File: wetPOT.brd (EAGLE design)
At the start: 38.1 x 12.7 mm, 2 parts

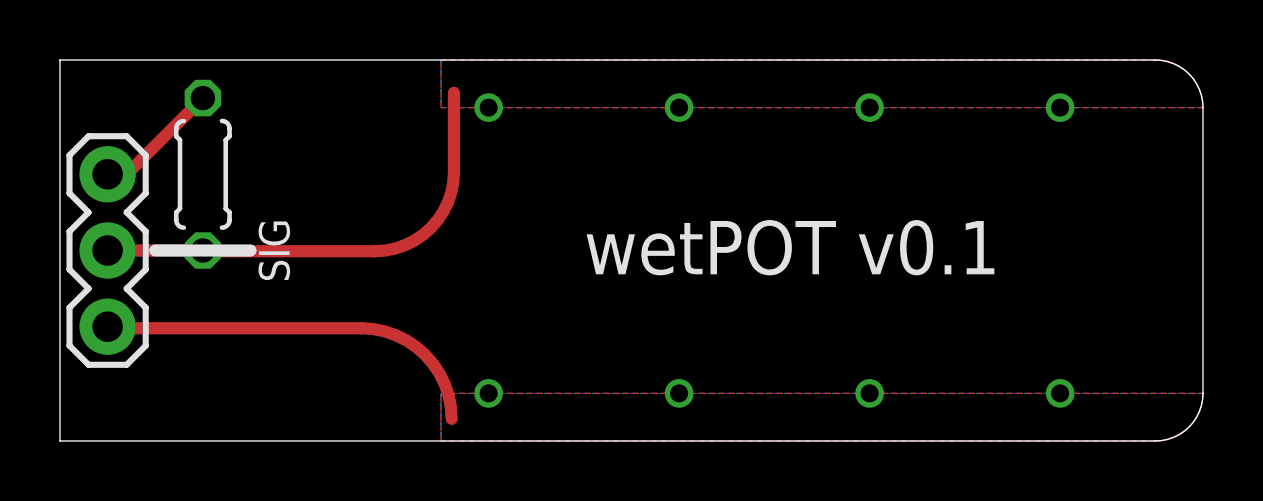
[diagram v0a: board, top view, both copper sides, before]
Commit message: Swap pin0 & pin1 to match servo wiring (Ground, VCC, Sig)
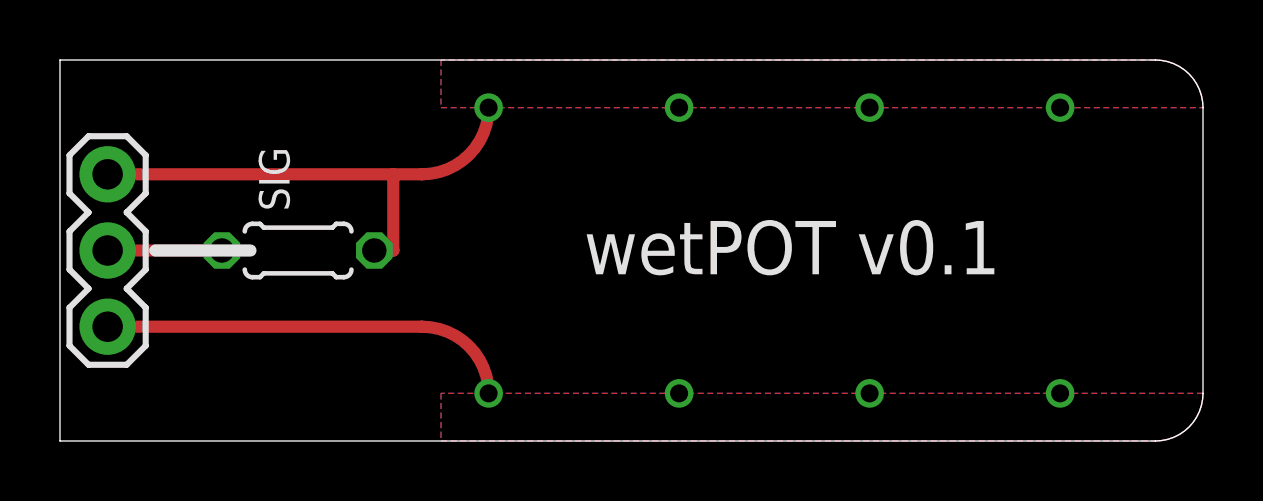
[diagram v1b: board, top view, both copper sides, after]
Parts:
- moved R1 4.07 mm to (7.94, 6.35), turned to 0 degrees
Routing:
- net PIN0: track 4.23 -> 16.8 mm, vias 0 -> 4
- net PIN1: track 15.2 -> 3.81 mm, vias 4 -> 0
- net PIN2: track 12.6 -> 13.6 mm
- added copper zone on layer 1, net PIN0
- added copper zone on layer 16, net PIN0
- removed copper zone on layer 1, net PIN1
- removed copper zone on layer 16, net PIN1
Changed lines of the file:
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@@
 <layer number="27" name="tValues" color="7" fill="1" visible="yes" active="yes"/>
 <layer number="28" name="bValues" color="7" fill="1" visible="yes" active="yes"/>
-<layer number="29" name="tStop" color="7" fill="3" visible="yes" active="yes"/>
-<layer number="30" name="bStop" color="7" fill="6" visible="yes" active="yes"/>
+<layer number="29" name="tStop" color="7" fill="3" visible="no" active="yes"/>
+<layer number="30" name="bStop" color="7" fill="6" visible="no" active="yes"/>
 <layer number="31" name="tCream" color="7" fill="4" visible="yes" active="yes"/>
 <layer number="32" name="bCream" color="7" fill="5" visible="yes" active="yes"/>
@@
 <wire x1="36.5125" y1="12.7" x2="0" y2="12.7" width="0" layer="20"/>
 <wire x1="0" y1="12.7" x2="0" y2="0" width="0" layer="20"/>
-<text x="7.14375" y="6.35" size="1.016" layer="121" rot="R90" align="center">SIG</text>
+<text x="7.14375" y="8.73125" size="1.016" layer="121" rot="R90" align="center">SIG</text>
 <wire x1="3.175" y1="6.35" x2="6.35" y2="6.35" width="0.4064" layer="121"/>
 <text x="17.4625" y="5.55625" size="1.778" layer="121">wetPOT v0.1</text>
+<polygon width="0.4064" layer="29">
+<vertex x="12.7" y="1.5875"/>
+<vertex x="38.1" y="1.5875" curve="-90"/>
+<vertex x="36.5125" y="0"/>
+<vertex x="12.7" y="0"/>
+</polygon>
+<polygon width="0.4064" layer="30">
+<vertex x="12.7" y="1.5875"/>
+<vertex x="12.7" y="0"/>
+<vertex x="36.5125" y="0" curve="90"/>
+<vertex x="38.1" y="1.5875"/>
+</polygon>
+<text x="34.13125" y="4.7625" size="1.4224" layer="122" rot="MR0">andrewparnell.com
+CC: BY-SA</text>
+<polygon width="0.4064" layer="30">
+<vertex x="12.7" y="12.7"/>
+<vertex x="12.7" y="11.1125"/>
+<vertex x="38.1" y="11.1125" curve="90"/>
+<vertex x="36.5125" y="12.7"/>
+</polygon>
 <polygon width="0.4064" layer="29">
 <vertex x="12.7" y="12.7"/>
@@
 <vertex x="36.5125" y="12.7"/>
 </polygon>
-<polygon width="0.4064" layer="29">
-<vertex x="12.7" y="1.5875"/>
-<vertex x="38.1" y="1.5875" curve="-90"/>
-<vertex x="36.5125" y="0"/>
-<vertex x="12.7" y="0"/>
-</polygon>
-<polygon width="0.4064" layer="30">
-<vertex x="12.7" y="11.1125"/>
-<vertex x="12.7" y="12.7"/>
-<vertex x="36.5125" y="12.7" curve="-90"/>
-<vertex x="38.1" y="11.1125"/>
-</polygon>
-<polygon width="0.4064" layer="30">
-<vertex x="12.7" y="1.5875"/>
-<vertex x="12.7" y="0"/>
-<vertex x="36.5125" y="0" curve="90"/>
-<vertex x="38.1" y="1.5875"/>
-</polygon>
-<text x="34.13125" y="4.7625" size="1.4224" layer="122" rot="MR0">andrewparnell.com
-CC: BY-SA</text>
 </plain>
 <attributes>
@@
 </autorouter>
 <elements>
-<element name="R1" library="resistor" package="0204/5" value="10k" x="4.7625" y="8.89" smashed="yes" rot="R90"/>
+<element name="R1" library="resistor" package="0204/5" value="10k" x="7.9375" y="6.35" smashed="yes"/>
 <element name="JP2" library="SparkFun-Connectors" package="1X03" value="" x="1.5875" y="3.81" smashed="yes" rot="R90">
 <attribute name="VALUE" x="4.7625" y="2.54" size="1.27" layer="27" rot="R90"/>
@@
 <contactref element="R1" pad="2"/>
 <contactref element="JP2" pad="3"/>
-<wire x1="1.5875" y1="8.89" x2="2.2225" y2="8.89" width="0.4064" layer="1"/>
-<wire x1="2.2225" y1="8.89" x2="4.7625" y2="11.43" width="0.4064" layer="1"/>
-</signal>
-<signal name="PIN1">
-<contactref element="R1" pad="1"/>
-<contactref element="JP2" pad="2"/>
-<wire x1="1.5875" y1="6.35" x2="4.7625" y2="6.35" width="0.4064" layer="1"/>
 <polygon width="0.4064" layer="1">
 <vertex x="12.7" y="12.7"/>
-<vertex x="36.5125" y="12.7" curve="-90"/>
-<vertex x="38.1" y="11.1125"/>
 <vertex x="12.7" y="11.1125"/>
-</polygon>
-<wire x1="4.826" y1="6.3246" x2="10.4902" y2="6.3246" width="0.4064" layer="1"/>
-<wire x1="10.4902" y1="6.3246" x2="13.1318" y2="8.9662" width="0.4064" layer="1" curve="90"/>
-<wire x1="13.1318" y1="8.9662" x2="13.1318" y2="11.6078" width="0.4064" layer="1"/>
+<vertex x="38.1" y="11.1125" curve="90"/>
+<vertex x="36.5125" y="12.7"/>
+</polygon>
 <polygon width="0.4064" layer="16">
 <vertex x="12.7" y="12.7"/>
@@
 <via x="26.9875" y="11.1125" extent="1-16" drill="0.6" shape="octagon"/>
 <via x="33.3375" y="11.1125" extent="1-16" drill="0.6" shape="octagon"/>
-<wire x1="26.9875" y1="11.1125" x2="33.3375" y2="11.1125" width="0" layer="19" extent="1-1"/>
-<wire x1="4.7625" y1="6.35" x2="4.826" y2="6.3246" width="0" layer="19" extent="1-1"/>
+<wire x1="1.5875" y1="8.89" x2="11.1125" y2="8.89" width="0.4064" layer="1"/>
+<wire x1="11.1125" y1="8.89" x2="12.065" y2="8.89" width="0.4064" layer="1"/>
+<wire x1="12.065" y1="8.89" x2="14.2875" y2="11.1125" width="0.4064" layer="1" curve="90"/>
+<wire x1="10.4775" y1="6.35" x2="11.1125" y2="6.35" width="0.4064" layer="1"/>
+<wire x1="11.1125" y1="6.35" x2="11.1125" y2="8.89" width="0.4064" layer="1"/>
+</signal>
+<signal name="PIN1">
+<contactref element="R1" pad="1"/>
+<contactref element="JP2" pad="2"/>
+<wire x1="1.5875" y1="6.35" x2="5.3975" y2="6.35" width="0.4064" layer="1"/>
 </signal>
 <signal name="N$4">
@@
 </signal>
 <signal name="PIN2">
-<wire x1="1.7018" y1="3.7592" x2="10.033" y2="3.7592" width="0.4064" layer="1"/>
-<wire x1="10.033" y1="3.7592" x2="13.0556" y2="0.7366" width="0.4064" layer="1" curve="-90"/>
+<contactref element="JP2" pad="1"/>
+<via x="20.6375" y="1.5875" extent="1-16" drill="0.6" shape="octagon"/>
+<via x="26.9875" y="1.5875" extent="1-16" drill="0.6" shape="octagon"/>
+<via x="33.3375" y="1.5875" extent="1-16" drill="0.6" shape="octagon"/>
+<via x="14.2875" y="1.5875" extent="1-16" drill="0.6" shape="octagon"/>
+<polygon width="0.4064" layer="16">
+<vertex x="12.7" y="1.5875"/>
+<vertex x="12.7" y="0"/>
+<vertex x="35.71875" y="0"/>
+<vertex x="36.5125" y="0" curve="90"/>
+<vertex x="38.1" y="1.5875"/>
+</polygon>
 <polygon width="0.4064" layer="1">
-<vertex x="12.7" y="1.5875"/>
-<vertex x="38.1" y="1.5875" curve="-90"/>
-<vertex x="36.5125" y="0"/>
-<vertex x="12.7" y="0"/>
-</polygon>
-<contactref element="JP2" pad="1"/>
-<polygon width="0.4064" layer="16">
 <vertex x="12.7" y="1.5875"/>
 <vertex x="12.7" y="0"/>
@@
 <vertex x="38.1" y="1.5875"/>
 </polygon>
-<via x="20.6375" y="1.5875" extent="1-16" drill="0.6" shape="octagon"/>
-<via x="26.9875" y="1.5875" extent="1-16" drill="0.6" shape="octagon"/>
-<via x="33.3375" y="1.5875" extent="1-16" drill="0.6" shape="octagon"/>
-<via x="14.2875" y="1.5875" extent="1-16" drill="0.6" shape="octagon"/>
-<wire x1="1.7018" y1="3.7592" x2="1.5875" y2="3.81" width="0" layer="19" extent="1-1"/>
+<wire x1="1.5875" y1="3.81" x2="12.065" y2="3.81" width="0.4064" layer="1"/>
+<wire x1="12.065" y1="3.81" x2="14.2875" y2="1.5875" width="0.4064" layer="1" curve="-90"/>
 </signal>
 </signals>
